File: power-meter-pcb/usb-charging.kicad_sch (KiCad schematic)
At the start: 17 parts, among them J4 Battery, J5 USB4120-03-C_REVA, U3 TPS613221ADBV, U4 TPD3E001DRLR

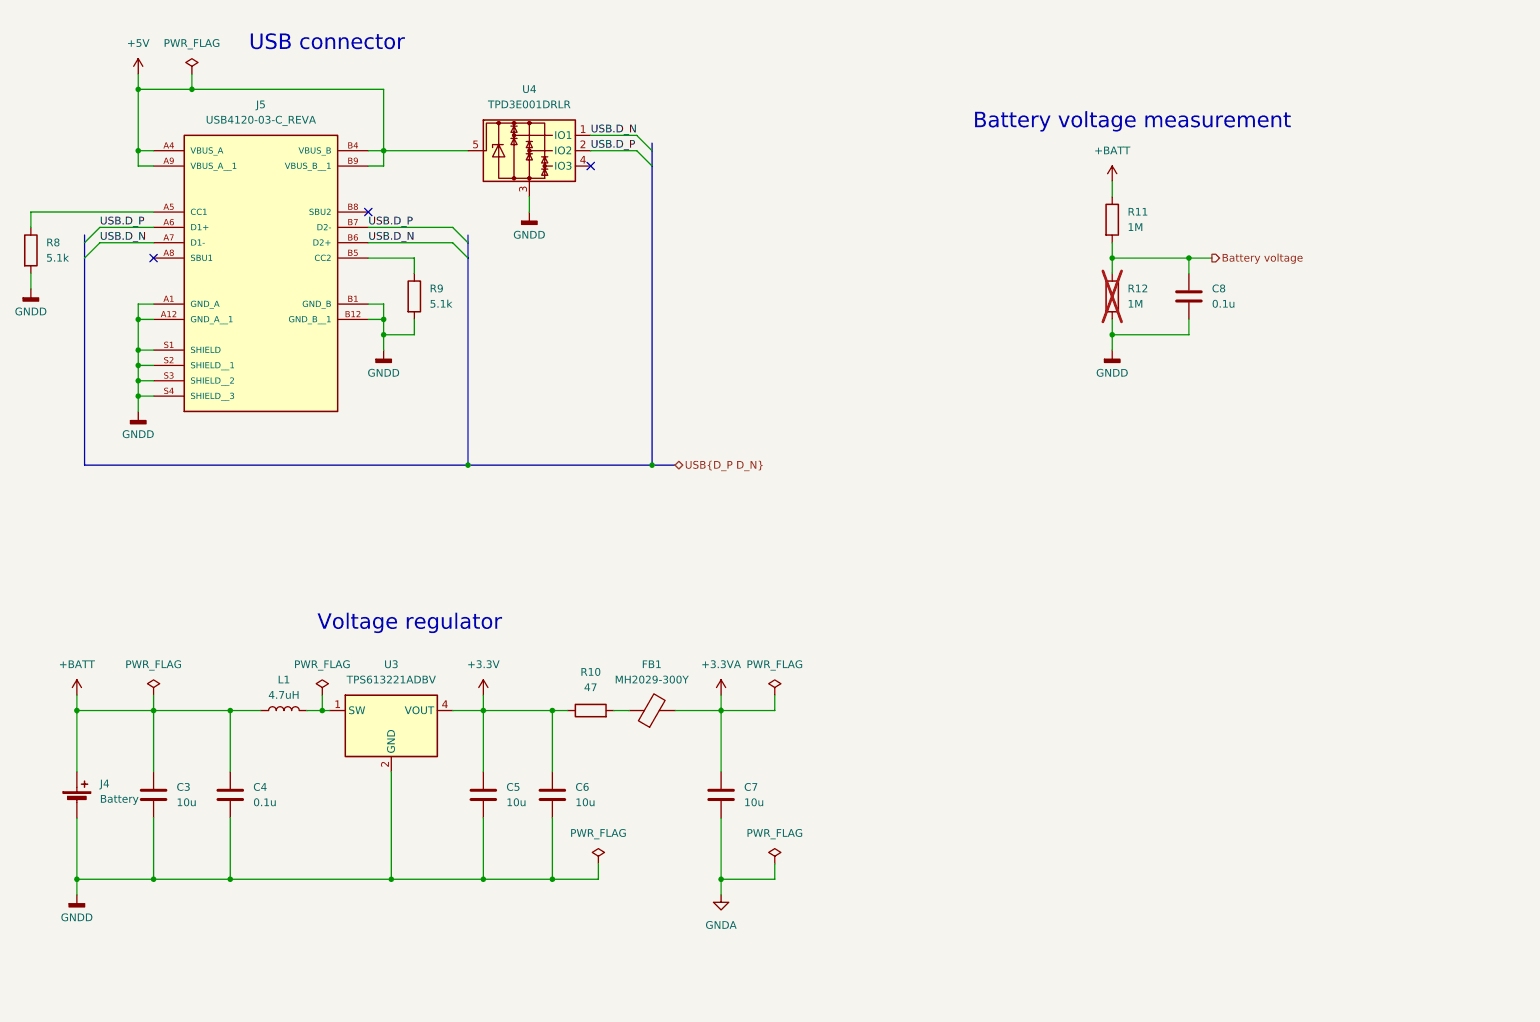
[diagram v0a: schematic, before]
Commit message: Uses a TPS61022 Voltage regulator - will change for easier soldering
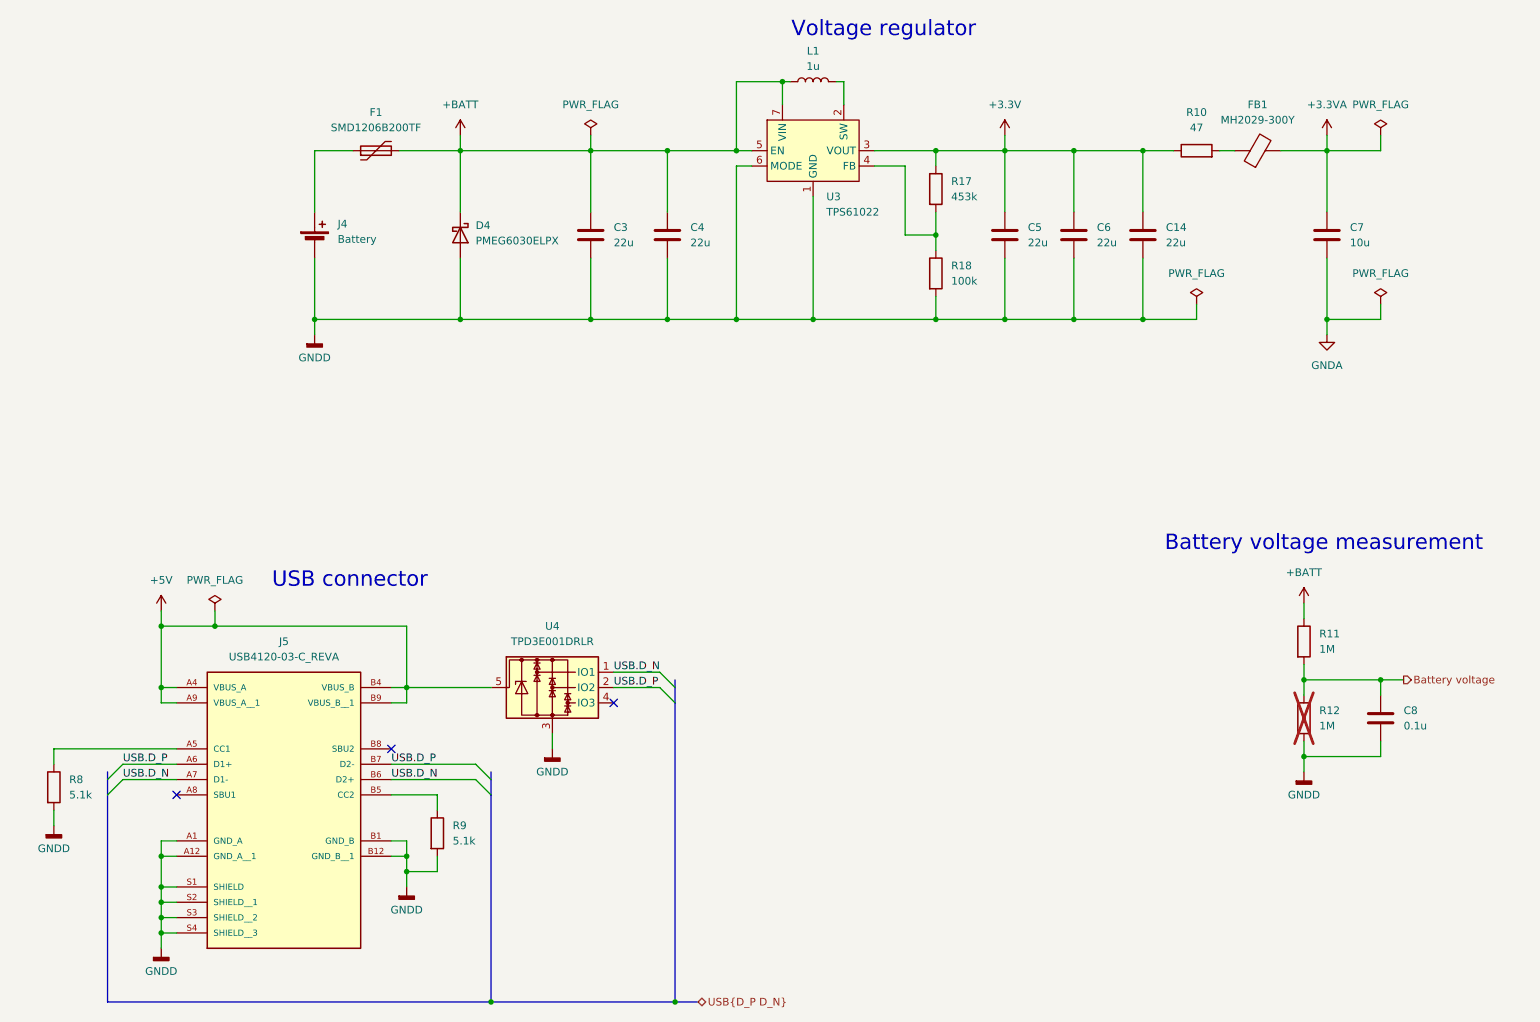
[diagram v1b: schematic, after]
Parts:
- removed U3: TPS613221ADBV, Package_TO_SOT_SMD:SOT-23-5, symbol Regulator_Switching:TPS613221ADBV
- added C14: 22u, Capacitor_SMD:C_0603_1608Metric_Pad1.08x0.95mm_HandSolder, symbol Device:C
- added D4: PMEG6030ELPX, Diode_SMD:D_SOD-128, symbol Device:D_Schottky
- added F1: SMD1206B200TF, Fuse:Fuse_1206_3216Metric_Pad1.42x1.75mm_HandSolder, symbol Device:Polyfuse
- added R17: 453k, Resistor_SMD:R_0603_1608Metric_Pad0.98x0.95mm_HandSolder, symbol Device:R
- added R18: 100k, Resistor_SMD:R_0603_1608Metric_Pad0.98x0.95mm_HandSolder, symbol Device:R
- added U3: TPS61022, Package_DFN_QFN:Texas_RWU0007A_VQFN-7_2x2mm_P0.5mm, symbol Converter_DCDC:TPS61022
- C3, C5, C6: value 10u -> 22u
- C4: value 0.1u -> 22u
- L1: value 4.7uH -> 1u; footprint Inductor_SMD:L_Murata_DFE201610P -> Inductor_SMD_Wurth:L_Wurth_WE-LQSH-4020; PlaceOnSecondary Yes -> (none)
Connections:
- net +3.3V: now also C14.1, R17.1, U3.3 (VOUT)
- net +BATT: now also D4.1 (K), F1.2, U3.5 (EN), U3.7 (VIN); no longer J4.1 (+)
- net GNDD: now also C14.2, D4.2 (A), R18.2, U3.1 (GND), U3.6 (MODE)
- net at L1.2: now also U3.2 (SW)
- new net: R17.2, R18.1, U3.4 (FB)
- new net: F1.1, J4.1 (+)
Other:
- moved on the sheet: C3, C4, C5, C6, C7, C8, FB1, J4, J5, R10, R11, R12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

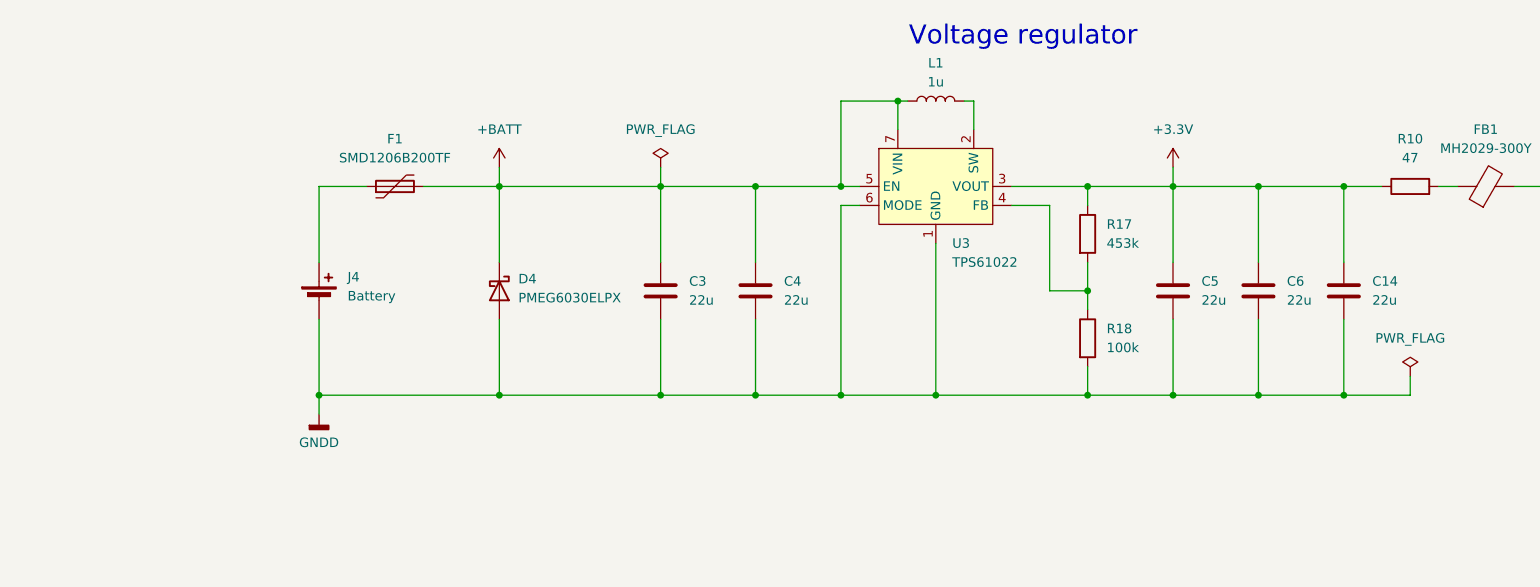
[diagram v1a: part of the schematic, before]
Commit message: New voltage regulator layout about done
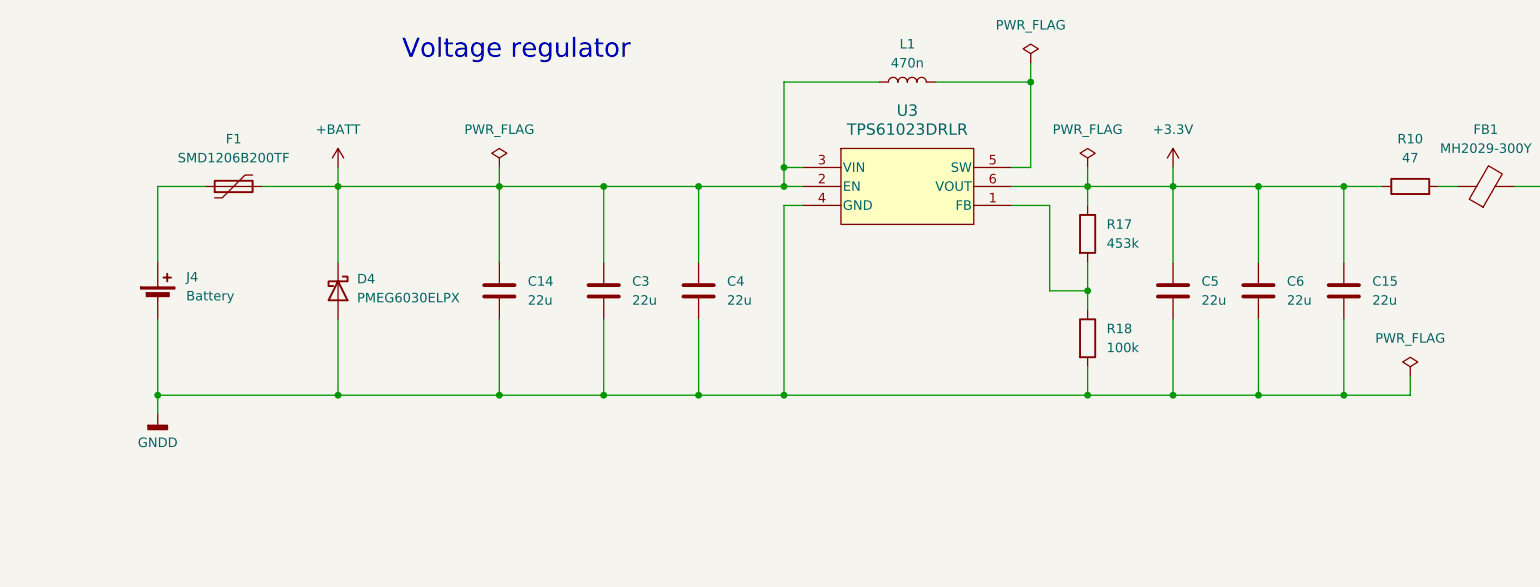
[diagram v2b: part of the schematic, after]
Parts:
- removed U3: TPS61022, Package_DFN_QFN:Texas_RWU0007A_VQFN-7_2x2mm_P0.5mm, symbol Converter_DCDC:TPS61022
- added C14: 22u, Capacitor_SMD:C_0603_1608Metric_Pad1.08x0.95mm_HandSolder, symbol Device:C
- added U3: TPS61023DRLR, DRL0006A, symbol TPS61023:TPS61023DRLR
- L1: value 1u -> 470n; footprint Inductor_SMD_Wurth:L_Wurth_WE-LQSH-4020 -> Inductor_SMD:L_Vishay_IHLP-1212
- renumbered C14 to C15
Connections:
- net +3.3V: now also U3.6 (VOUT)
- net +BATT: now also C14.1, U3.2 (EN), U3.3 (VIN)
- net GNDD: now also C14.2, U3.4 (GND)
- net at R17.2, R18.1: now also U3.1 (FB)
- net at L1.2: now also U3.5 (SW)
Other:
- moved on the sheet: C3, C4, D4, F1, J4, L1

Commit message: PCB modifications about done
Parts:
- U3: footprint DRL0006A -> TPS61023DRLR:DRL0006A
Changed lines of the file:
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@@
 	(title_block
 		(title "Cycling power meter FYP - USB and power supply")
-		(date "2024-08-08")
-		(rev "V1.1.0")
+		(date "2024-09-10")
+		(rev "V1.1.1")
 		(company "Monash Human Power - Jotham Gates & Oscar Varney")
 	)
@@
 			)
 		)
-		(property "Footprint" "DRL0006A"
+		(property "Footprint" "TPS61023DRLR:DRL0006A"
 			(at 153.162 56.896 0)
 			(effects

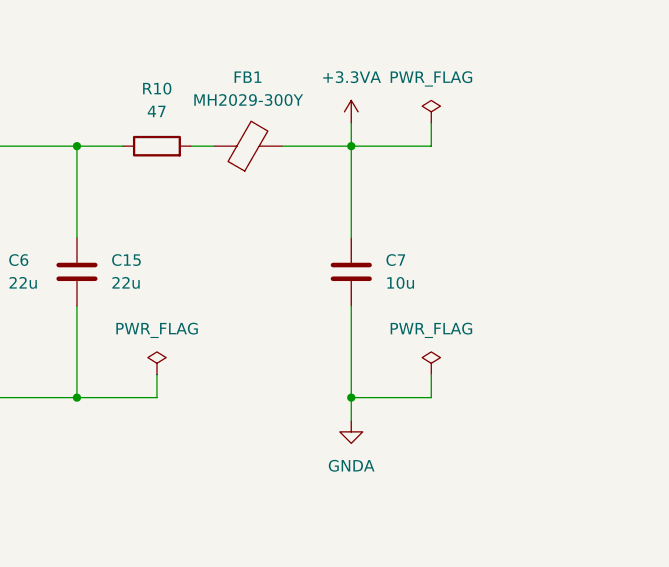
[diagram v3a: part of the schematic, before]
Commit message: Sorting out parts to order and component changes
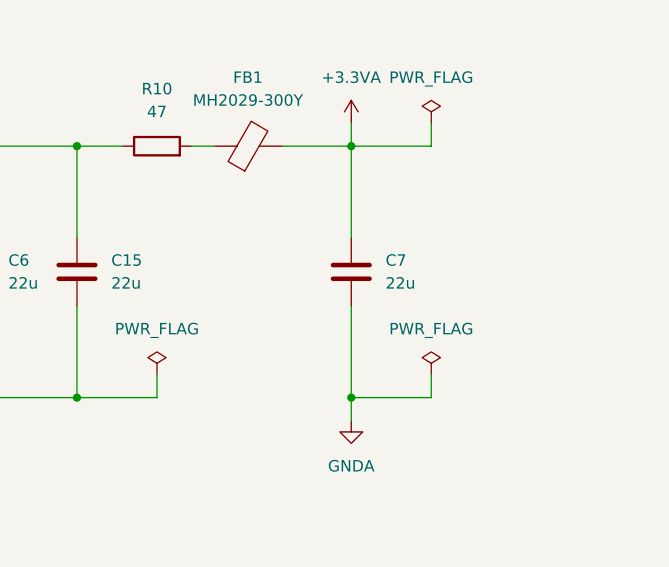
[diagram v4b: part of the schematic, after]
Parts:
- C14, C15, C3, C4, C5, C6: SchematicVersionModified (none) -> V1.1.1
- C7: value 10u -> 22u; SchematicVersionModified (none) -> V1.1.1
- C8, FB1, J4, J5, R10, R11, R12, R8, R9, U4: SchematicVersionModified (none) -> V1.0.4
- D4, F1: PlaceOnSecondary (none) -> No; SchematicVersionModified (none) -> V1.1.1
- L1, R17, R18, U3: PlaceOnSecondary (none) -> Yes; SchematicVersionModified (none) -> V1.1.1

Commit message: Fixed USB data pin polarity in one orientation, added test point
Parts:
- added TP1: 5V, TestPoint:TestPoint_Pad_1.5x1.5mm, symbol Connector:TestPoint
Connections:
- net +5V: now also TP1.1
- net USB.D_N: now also J5.B7 (D2-), U4.2 (IO2); no longer J5.B6 (D2+), U4.1 (IO1)
- net USB.D_P: now also J5.B6 (D2+), U4.1 (IO1); no longer J5.B7 (D2-), U4.2 (IO2)
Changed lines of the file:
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@@
 	)
 	(junction
+		(at 67.31 125.73)
+		(diameter 0)
+		(color 0 0 0 0)
+	)
+	(junction
 		(at 49.53 171.45)
 		(diameter 0)
@@
 	(wire
 		(pts
+			(xy 67.31 124.46) (xy 67.31 125.73)
+		)
+		(stroke
+			(width 0)
+			(type default)
+		)
+	)
+	(wire
+		(pts
 			(xy 234.95 46.99) (xy 242.57 46.99)
 		)
@@
 	(wire
 		(pts
-			(xy 58.42 125.73) (xy 90.17 125.73)
+			(xy 58.42 125.73) (xy 67.31 125.73)
 		)
 		(stroke
@@
 	(wire
 		(pts
+			(xy 67.31 125.73) (xy 90.17 125.73)
+		)
+		(stroke
+			(width 0)
+			(type default)
+		)
+	)
+	(wire
+		(pts
 			(xy 212.09 74.93) (xy 220.98 74.93)
 		)
@@
 	(text "USB connector"
 		(exclude_from_sim no)
-		(at 80.772 118.11 0)
+		(at 64.516 111.76 0)
 		(effects
 			(font
@@
 		)
 	)
-	(label "USB.D_N"
+	(label "USB.D_P"
 		(at 124.46 133.35 0)
 		(fields_autoplaced yes)
@@
 		)
 	)
-	(label "USB.D_P"
+	(label "USB.D_N"
 		(at 87.63 148.59 0)
 		(fields_autoplaced yes)
@@
 		)
 	)
-	(label "USB.D_P"
+	(label "USB.D_N"
 		(at 124.46 135.89 0)
 		(fields_autoplaced yes)
@@
 		)
 	)
-	(label "USB.D_N"
+	(label "USB.D_P"
 		(at 87.63 151.13 0)
 		(fields_autoplaced yes)
@@
 					(unit 1)
 				)
+			)
+		)
+	)
+	(symbol
+		(lib_id "Connector:TestPoint")
+		(at 67.31 124.46 0)
+		(unit 1)
+		(exclude_from_sim no)
+		(in_bom yes)
+		(on_board yes)
+		(dnp no)
+		(fields_autoplaced yes)
+		(property "Reference" "TP1"
+			(at 69.85 119.8879 0)
+			(effects
+				(font
+					(size 1.27 1.27)
+				)
+				(justify left)
+			)
+		)
+		(property "Value" "5V"
+			(at 69.85 122.4279 0)
+			(effects
+				(font
+					(size 1.27 1.27)
+				)
+				(justify left)
+			)
+		)
+		(property "Footprint" "TestPoint:TestPoint_Pad_1.5x1.5mm"
+			(at 72.39 124.46 0)
+			(effects
+				(font
+					(size 1.27 1.27)
+				)
+				(hide yes)
+			)
+		)
+		(property "Datasheet" "~"
+			(at 72.39 124.46 0)
+			(effects
+				(font
+					(size 1.27 1.27)
+				)
+				(hide yes)
+			)
+		)
+		(property "Description" "test point"
+			(at 67.31 124.46 0)
+			(effects
+				(font
+					(size 1.27 1.27)
+				)
+				(hide yes)
+			)
+		)
+		(pin "1"
+		)
+		(instances
+			(project ""
+				(path "/73d1dc3f-3725-4767-8c11-2d32e15ee0d6/4fb726d4-a68e-4ad8-a718-58b82440e761"
+					(reference "TP1")
+					(unit 1)
+				)
